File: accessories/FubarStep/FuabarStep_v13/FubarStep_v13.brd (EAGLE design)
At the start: 115.6 x 49.5 mm, 82 parts, among them IC2 SN754410NE, IC3 SN754410NE, U1 FUBARINO_SD, U2 FUBARINO_MINI, U3 OKI-78SR-5/1.5-W36H-C, X1 DC21MMX

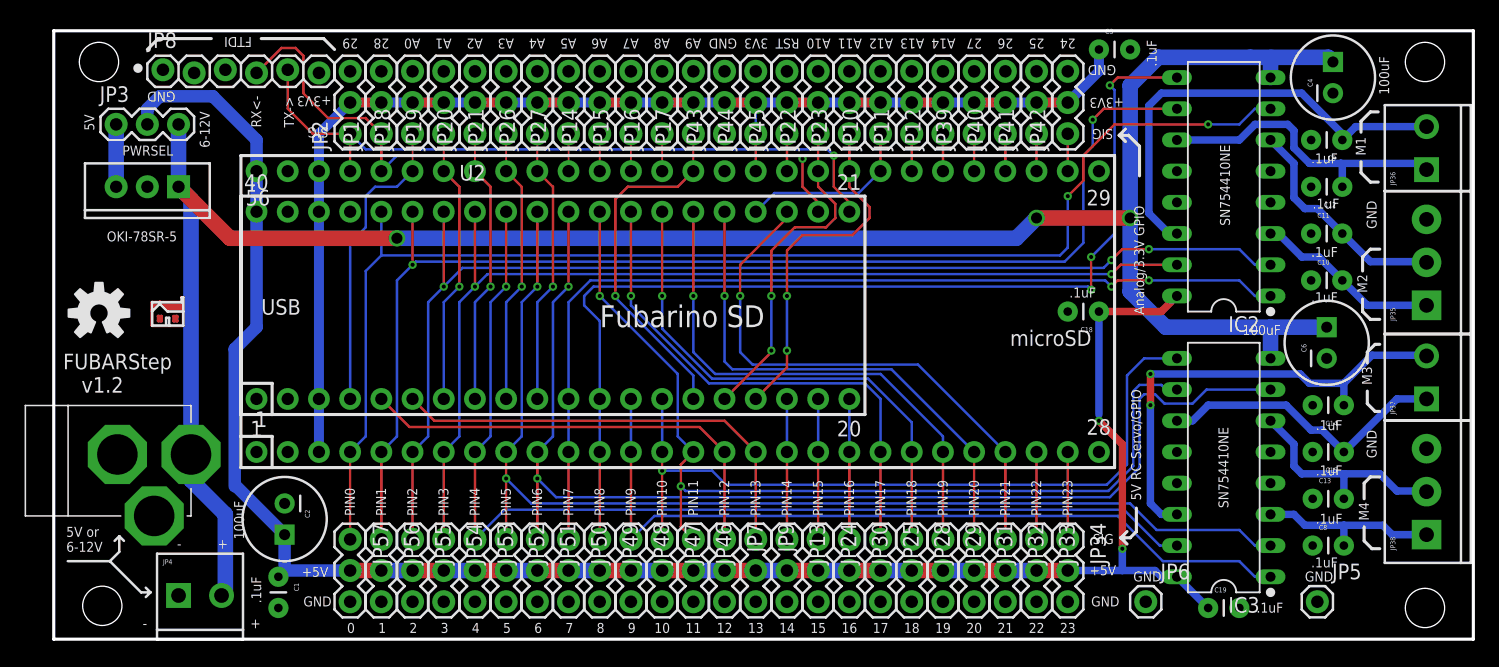
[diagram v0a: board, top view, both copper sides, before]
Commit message: Version 1.3 ready for review. Added pull down resistors to H-Bridge inputs, tweaked part placement for better assembly and silk screen for more information and readability.
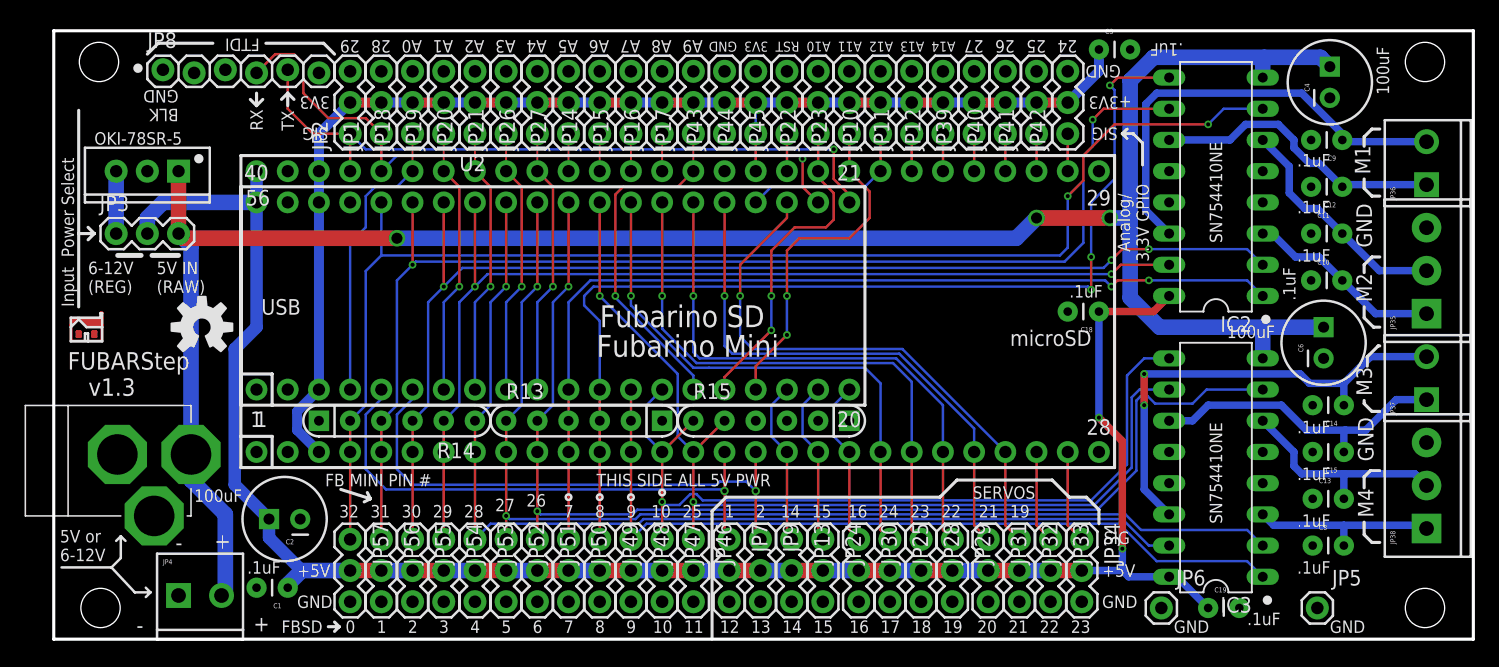
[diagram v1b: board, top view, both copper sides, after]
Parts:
- added R13, R14, R15: 10K, SparkFun-Resistors:RPACK-SIP-PTH-5
- moved JP3 8.89 mm to (5.08, 33.0)
- moved LOGO1 8.46 mm to (12.1, 25.4)
- moved U$1 6.73 mm to (2.67, 24.3)
- moved JP6 1.37 mm to (90.2, 2.54)
- moved U3 1.27 mm to (7.62, 38.1)
- moved JP36 1.23 mm to (111.8, 37.0)
- moved C1 1.17 mm to (19.1, 4.19), turned to 180 degrees
- moved JP32 1.14 mm to (78.6, 8.13)
- moved JP33 1.14 mm to (81.2, 8.13)
- moved JP34 1.14 mm to (83.7, 8.13)
- moved JP31 1.14 mm to (76.1, 8.13)
- moved JP25 0.76 mm to (68.1, 8.13)
- moved JP28 0.76 mm to (70.6, 8.13)
- moved JP29 0.76 mm to (73.2, 8.13)
- moved JP30 0.76 mm to (65.5, 8.13)
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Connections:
- net GND: now also R13.P$1, R14.P$1, R15.P$1
- net M1A1: now also R14.P$4
- net M1A2: now also R14.P$2
- net M1A3: now also R14.P$3
- net M1A4: now also R14.P$5
- net M1EN12: now also R13.P$4
- net M1EN34: now also R13.P$3
- net M2A1: now also R13.P$6
- net M2A2: now also R13.P$5
- net M2A3: now also R15.P$5
- net M2A4: now also R14.P$6
- net M2EN12: now also R13.P$2
- net M2EN34: now also R15.P$6
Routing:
- net PIN13: track 36.8 -> 44.4 mm, vias 0 -> 1
- net PIN12: track 36.8 -> 44.2 mm, vias 0 -> 1
- net M2EN34: track 62.3 -> 67.8 mm
- net VIN: track 175.8 -> 170.6 mm
- net +5V: track 155.5 -> 151.2 mm
- net PIN18: track 42.5 -> 45.5 mm
- net PIN19: track 43.0 -> 45.5 mm
- net PIN16: track 11.4 -> 13.6 mm
- net PIN15: track 11.4 -> 13.4 mm
- net PIN14: track 11.4 -> 13.4 mm
- net PIN17: track 42.5 -> 44.3 mm
- net M2A3: track 78.5 -> 80.3 mm
- net PIN20: track 42.7 -> 44.3 mm
- net RX: track 58.5 -> 56.9 mm
- net 3.3V: track 98.9 -> 100.4 mm
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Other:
- board text added: "30"
- board text added: "31"
- board text added: "32"
- board text added: "5V IN (RAW)"
- board text added: "6-12V (REG)"
- board text added: "Analog/ 3.3V GPIO"
- board text added: "BLK GND"
- board text added: "FB MINI PIN #"
- board text added: "FBSD"
- board text added: "FUBARStep v1.3"
- board text added: "Fubarino Mini"
- board text added: "Input Power Select"
- board text added: "RX"
- board text added: "SERVOS"
- board text added: "THIS SIDE ALL 5V PWR"
- board text added: "TX"
- board text removed: "5V"
- board text removed: "5V RC Servo/GPIO"
- board text removed: "6-12V"
- board text removed: "Analog/3.3V GPIO"
- board text removed: "FUBARStep v1.2"
- board text removed: "PIN0"
- board text removed: "PIN1"
- board text removed: "PIN10"
- board text removed: "PIN11"
- board text removed: "PIN12"
- board text removed: "PIN13"
- board text removed: "PIN14"
- board text removed: "PIN15"
- board text removed: "PIN16"
- board text removed: "PIN17"
- board text removed: "PIN18"
- board text removed: "PIN19"
- board text removed: "PIN2"
- board text removed: "PIN20"
- board text removed: "PIN21"
- board text removed: "PIN22"
- board text removed: "PIN23"
- board text removed: "PIN3"
- board text removed: "PIN4"
- board text removed: "PIN5"
- board text removed: "PIN6"
- board text removed: "PIN7"
- board text removed: "PIN8"
- board text removed: "PIN9"
- board text removed: "PWRSEL"
- board text removed: "RX<-"
- board text removed: "TX->"
